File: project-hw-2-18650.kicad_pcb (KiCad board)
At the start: 2 copper layers, 98 x 44 mm, 15 parts, among them J1 2060-452_998-404, U1 TPS62933

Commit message: add: version
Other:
- board text added: "v1.0.0"
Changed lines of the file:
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@@
 		(layer "Edge.Cuts")
+	)
+	(gr_text "v1.0.0"
+		(at 104 56.5 0)
+		(layer "B.SilkS")
+		(effects
+			(font
+				(face "FreeSans")
+				(size 2 2)
+				(thickness 0.1)
+			)
+			(justify left bottom mirror)
+		)
+		(render_cache "v1.0.0" 0
+			(polygon
+				(pts
+					(xy 103.197906 56.16) (xy 103.454361 56.16) (xy 103.971667 54.690635) (xy 103.707397 54.690635)
+					(xy 103.313677 55.88254) (xy 102.896999 54.690635) (xy 102.632728 54.690635)
+				)
+			)
+			(polygon
+				(pts
+					(xy 101.883879 54.721898) (xy 102.325471 54.721898) (xy 102.325471 54.534319) (xy 102.224949 54.520386)
+					(xy 102.125386 54.501786) (xy 102.025403 54.474163) (xy 101.95129 54.438576) (xy 101.884035 54.363005)
+					(xy 101.837458 54.269544) (xy 101.803424 54.172656) (xy 101.799371 54.159162) (xy 101.636217 54.159162)
+					(xy 101.636217 56.16) (xy 101.883879 56.16)
+				)
+			)
+			(polygon
+				(pts
+					(xy 100.539567 55.878632) (xy 100.539567 56.16) (xy 100.83217 56.16) (xy 100.83217 55.878632)
+				)
+			)
+			(polygon
+				(pts
+					(xy 99.66343 54.163463) (xy 99.759944 54.181632) (xy 99.850106 54.218191) (xy 99.932868 54.271514)
+					(xy 99.960347 54.293429) (xy 100.030819 54.36545) (xy 100.087718 54.446392) (xy 100.091726 54.453189)
+					(xy 100.13648 54.547414) (xy 100.169052 54.643775) (xy 100.194696 54.744368) (xy 100.199783 54.768411)
+					(xy 100.21685 54.869161) (xy 100.228665 54.977238) (xy 100.234695 55.077817) (xy 100.236706 55.184005)
+					(xy 100.236544 55.21552) (xy 100.232651 55.336836) (xy 100.223568 55.450565) (xy 100.209295 55.556708)
+					(xy 100.189832 55.655264) (xy 100.158205 55.767789) (xy 100.118467 55.868461) (xy 100.070621 55.957278)
+					(xy 100.049257 55.989398) (xy 99.97793 56.073324) (xy 99.89575 56.1386) (xy 99.802717 56.185225)
+					(xy 99.69883 56.213201) (xy 99.584089 56.222526) (xy 99.544928 56.221501) (xy 99.434521 56.206131)
+					(xy 99.334726 56.172317) (xy 99.245545 56.120058) (xy 99.166977 56.049356) (xy 99.099023 55.960209)
+					(xy 99.088714 55.943555) (xy 99.042082 55.853431) (xy 99.00363 55.751882) (xy 98.97336 55.638907)
+					(xy 98.955034 55.540302) (xy 98.941944 55.434385) (xy 98.93409 55.321155) (xy 98.931472 55.200614)
+					(xy 98.931926 55.178143) (xy 99.184508 55.178143) (xy 99.186049 55.280328) (xy 99.192313 55.398357)
+					(xy 99.203394 55.505604) (xy 99.219294 55.602071) (xy 99.244733 55.703599) (xy 99.283182 55.802428)
+					(xy 99.323882 55.870824) (xy 99.399488 55.946884) (xy 99.492559 55.991106) (xy 99.589951 56.003684)
+					(xy 99.703376 55.983732) (xy 99.797576 55.923876) (xy 99.859095 55.84726) (xy 99.90831 55.745105)
+					(xy 99.937147 55.65173) (xy 99.959063 55.543989) (xy 99.974058 55.421882) (xy 99.982132 55.28541)
+					(xy 99.98367 55.186448) (xy 99.98328 55.136709) (xy 99.977427 54.996968) (xy 99.96455 54.871439)
+					(xy 99.944649 54.76012) (xy 99.907188 54.6338) (xy 99.85724 54.532745) (xy 99.794806 54.456953)
+					(xy 99.699203 54.397741) (xy 99.584089 54.378004) (xy 99.535702 54.381129) (xy 99.428393 54.416292)
+					(xy 99.340594 54.490523) (xy 99.284403 54.578039) (xy 99.240699 54.690558) (xy 99.216115 54.791357)
+					(xy 99.198555 54.906221) (xy 99.188019 55.03515) (xy 99.184508 55.178143) (xy 98.931926 55.178143)
+					(xy 98.934021 55.0745) (xy 98.941669 54.956523) (xy 98.954415 54.846683) (xy 98.97226 54.744979)
+					(xy 99.008588 54.607678) (xy 99.056387 54.488684) (xy 99.115658 54.387997) (xy 99.1864 54.305616)
+					(xy 99.268615 54.241543) (xy 99.362301 54.195776) (xy 99.467459 54.168315) (xy 99.584089 54.159162)
+				)
+			)
+			(polygon
+				(pts
+					(xy 98.284717 55.878632) (xy 98.284717 56.16) (xy 98.57732 56.16) (xy 98.57732 55.878632)
+				)
+			)
+			(polygon
+				(pts
+					(xy 97.40858 54.163463) (xy 97.505094 54.181632) (xy 97.595257 54.218191) (xy 97.678018 54.271514)
+					(xy 97.705497 54.293429) (xy 97.775969 54.36545) (xy 97.832868 54.446392) (xy 97.836876 54.453189)
+					(xy 97.88163 54.547414) (xy 97.914202 54.643775) (xy 97.939846 54.744368) (xy 97.944933 54.768411)
+					(xy 97.962 54.869161) (xy 97.973815 54.977238) (xy 97.979846 55.077817) (xy 97.981856 55.184005)
+					(xy 97.981694 55.21552) (xy 97.977801 55.336836) (xy 97.968718 55.450565) (xy 97.954445 55.556708)
+					(xy 97.934982 55.655264) (xy 97.903355 55.767789) (xy 97.863617 55.868461) (xy 97.815771 55.957278)
+					(xy 97.794407 55.989398) (xy 97.72308 56.073324) (xy 97.6409 56.1386) (xy 97.547867 56.185225)
+					(xy 97.44398 56.213201) (xy 97.329239 56.222526) (xy 97.290078 56.221501) (xy 97.179671 56.206131)
+					(xy 97.079876 56.172317) (xy 96.990695 56.120058) (xy 96.912127 56.049356) (xy 96.844173 55.960209)
+					(xy 96.833864 55.943555) (xy 96.787232 55.853431) (xy 96.74878 55.751882) (xy 96.71851 55.638907)
+					(xy 96.700184 55.540302) (xy 96.687094 55.434385) (xy 96.67924 55.321155) (xy 96.676622 55.200614)
+					(xy 96.677076 55.178143) (xy 96.929658 55.178143) (xy 96.931199 55.280328) (xy 96.937463 55.398357)
+					(xy 96.948544 55.505604) (xy 96.964444 55.602071) (xy 96.989883 55.703599) (xy 97.028332 55.802428)
+					(xy 97.069032 55.870824) (xy 97.144638 55.946884) (xy 97.237709 55.991106) (xy 97.335101 56.003684)
+					(xy 97.448526 55.983732) (xy 97.542726 55.923876) (xy 97.604245 55.84726) (xy 97.65346 55.745105)
+					(xy 97.682297 55.65173) (xy 97.704213 55.543989) (xy 97.719208 55.421882) (xy 97.727282 55.28541)
+					(xy 97.72882 55.186448) (xy 97.72843 55.136709) (xy 97.722577 54.996968) (xy 97.7097 54.871439)
+					(xy 97.689799 54.76012) (xy 97.652338 54.6338) (xy 97.60239 54.532745) (xy 97.539956 54.456953)
+					(xy 97.444353 54.397741) (xy 97.329239 54.378004) (xy 97.280852 54.381129) (xy 97.173543 54.416292)
+					(xy 97.085744 54.490523) (xy 97.029553 54.578039) (xy 96.985849 54.690558) (xy 96.961265 54.791357)
+					(xy 96.943705 54.906221) (xy 96.93317 55.03515) (xy 96.929658 55.178143) (xy 96.677076 55.178143)
+					(xy 96.679171 55.0745) (xy 96.686819 54.956523) (xy 96.699566 54.846683) (xy 96.717411 54.744979)
+					(xy 96.753738 54.607678) (xy 96.801537 54.488684) (xy 96.860808 54.387997) (xy 96.93155 54.305616)
+					(xy 97.013765 54.241543) (xy 97.107451 54.195776) (xy 97.212609 54.168315) (xy 97.329239 54.159162)
+				)
+			)
+		)
 	)
 	(via

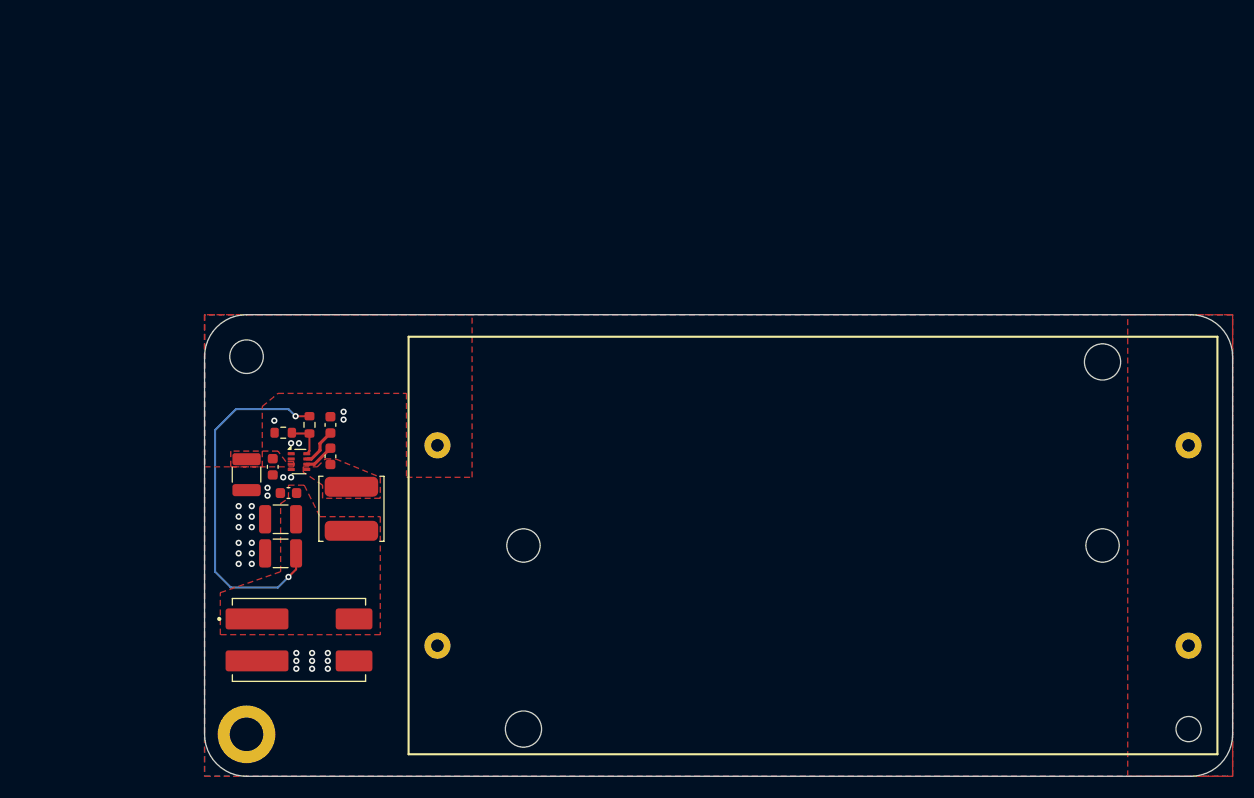
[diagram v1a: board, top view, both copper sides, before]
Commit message: pcb: place efuse
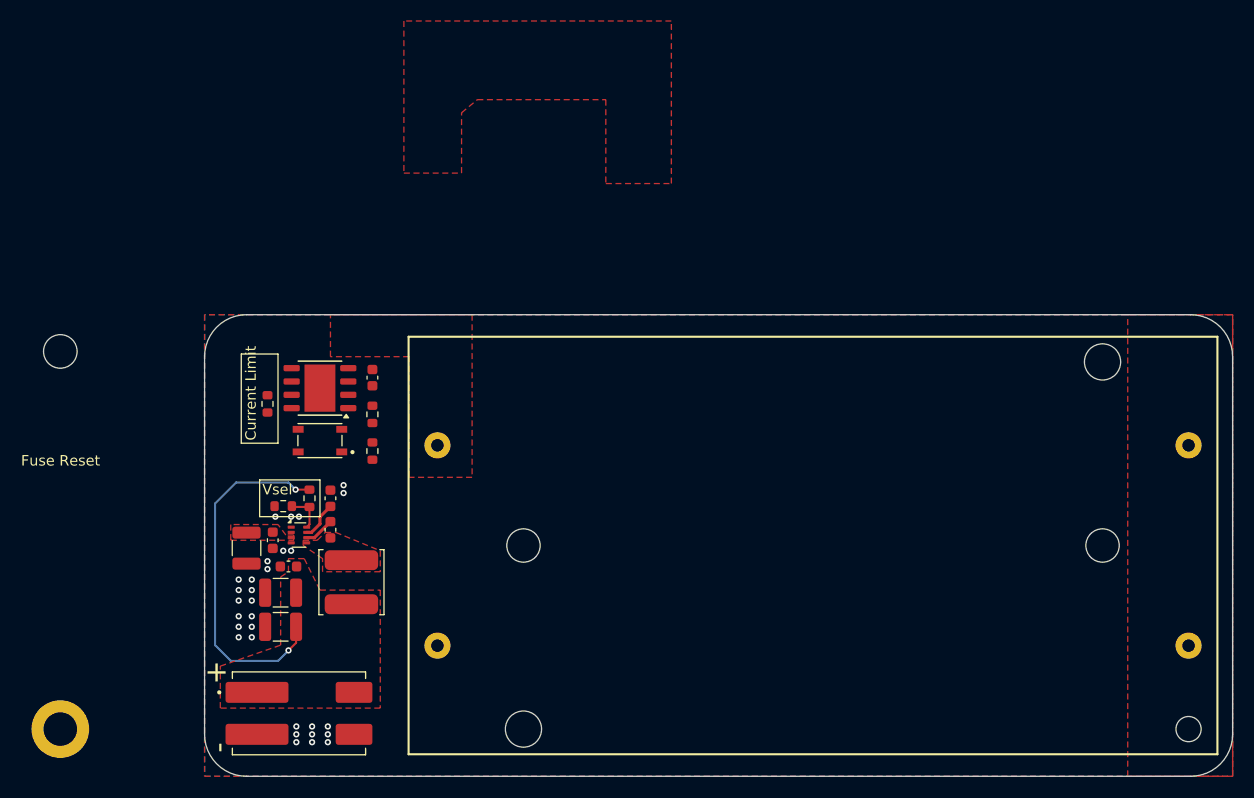
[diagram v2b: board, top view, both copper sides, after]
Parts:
- added C8: 0.1uF, Capacitor_SMD:C_0603_1608Metric, F.Cu at (34.0, 22.0)
- added R3: 31.6k, Resistor_SMD:R_0603_1608Metric, F.Cu at (34.0, 25.5)
- added R4: 100k, Resistor_SMD:R_0603_1608Metric, F.Cu at (34.0, 29.0)
- added R5: 470, SMD:0603_1608Metric_DNI_NoPaste, F.Cu at (24.0, 24.5)
- added SW1: PTS810_SJM_250_SMTR_LFS, PTS810-SJM-250-SMTR-LFS:SW_PTS810_SJM_250_SMTR_LFS, F.Cu at (29.0, 28.0)
- added U2: TPS259630, SO:TI_SO-PowerPAD-8, F.Cu at (29.0, 23.0)
- C1: value 10uF -> 22uF
- moved H1 17.8 mm to (4.25, 19.5)
- moved H2 17.8 mm to (4.25, 55.5)
- moved C1 7.00 mm to (22.0, 38.2)
- moved C2 7.00 mm to (24.5, 37.5)
- moved C3 7.00 mm to (30.0, 33.5)
- moved C4 7.00 mm to (30.0, 36.5)
- moved C5 7.00 mm to (26.0, 40.0)
- moved C6 7.00 mm to (25.2, 45.8)
- moved C7 7.00 mm to (25.2, 42.5)
- moved J1 7.00 mm to (27.0, 54.0)
- moved L1 7.00 mm to (32.0, 41.5)
- moved R1 7.00 mm to (28.0, 33.5)
- moved R2 7.00 mm to (25.5, 34.2)
- moved U1 7.00 mm to (27.0, 37.0)
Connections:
- C1 pad 1: +BATT -> /TPS6293x Converter/Vin
- C2 pad 1: +BATT -> /TPS6293x Converter/Vin
- U1 pad 3: +BATT -> /TPS6293x Converter/Vin
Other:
- board text added: "+"
- board text added: "-"
- board text added: "Current Limit"
- board text added: "Fuse Reset"
- board text added: "Vsel"

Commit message: pcb: first complete routing
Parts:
- removed H1: MountingHole, MountingHole:MountingHole_3.2mm_M3_ISO14580
- removed H2: MountingHole_Pad, MountingHole:MountingHole_3.2mm_M3_ISO14580_Pad
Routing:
- net Net-(U2-EN/UVLO): track 0.00 -> 14.2 mm
- net +BATT: track 0.00 -> 7.76 mm, vias 0 -> 1
- net Net-(U2-ILM): track 0.00 -> 2.32 mm
- net GND: vias 30 -> 41
- added copper zone on F.Cu, net /TPS6293x Converter/Vin
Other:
- board text removed: "Fuse Reset"
